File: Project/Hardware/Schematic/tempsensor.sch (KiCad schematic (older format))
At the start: 0 parts

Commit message: Lade till krets för temperatursensor.
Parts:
- added C?: 0.1u, symbol Device:C
- added R? (x6): R, symbol Device:R
- added TH?: PT1000, symbol Sensor_Temperature:PT1000
- added U?: MAX4460ESA+, 21-0041B_8, symbol PASC:MAX4460ESA+
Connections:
- new net: R?.2, TH?.1
- new net +3V3: C?.1, R?.1, R?.2, U?.7 (VDD)
- new net GND: C?.2, R?.1, R?.2, TH?.2, U?.2 (GND)
- new net INAMPFB: R?.1, R?.2, U?.8 (FB)
- new net TEMPOUT: R?.1, U?.1 (OUT)
- new net WBRIDGE+: R?.1, R?.1, U?.3 (IN+)
- new net WBRIDGE-: R?.2, R?.2, U?.6 (IN-)
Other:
- note added: "Instrumentation Amplifier"
- note added: "Set gain: 1 + R2/R1; R1 + R2 approx. = 100k\nR2 between OUT and FB,\nR1 between FB and GND."
- note added: "Wheatstone Bridge for Pt1000 thermistor.\n"

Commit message: Lade till komponentvärden i kretsschemat för temperatursensorkretsen
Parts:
- added R? (x2): 270k, symbol Device:R
- added R?: 820, symbol Device:R
- R?: value R -> 1k
- R? (x2): value R -> 8.2k
- R?: value R -> 1.8k
- R?: value R -> 100k
- R?: value R -> 2.7k
- U?: symbol PASC:MAX4460ESA+ -> lab-rescue:MAX4460ESA+-PASC
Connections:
- net +3V3: now also R?.1, R?.2
- net GND: now also R?.2; no longer R?.2
- net WBRIDGE+: now also R?.1
- net WBRIDGE-: now also R?.2
- new net: R?.1, R?.2
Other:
- moved on the sheet: R?, TH?
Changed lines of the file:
@@
 L Sensor_Temperature:PT1000 TH?
 U 1 1 5C561FEF
-P 3000 2600
-F 0 "TH?" H 3098 2646 50  0000 L CNN
-F 1 "PT1000" H 3098 2555 50  0000 L CNN
-F 2 "" H 3000 2650 50  0001 C CNN
-F 3 "https://www.heraeus.com/media/media/group/doc_group/products_1/hst/sot_to/de_15/to_92_d.pdf" H 3000 2650 50  0001 C CNN
-	1    3000 2600
+P 3200 2600
+F 0 "TH?" H 3298 2646 50  0000 L CNN
+F 1 "PT1000" H 3298 2555 50  0000 L CNN
+F 2 "" H 3200 2650 50  0001 C CNN
+F 3 "https://www.heraeus.com/media/media/group/doc_group/products_1/hst/sot_to/de_15/to_92_d.pdf" H 3200 2650 50  0001 C CNN
+	1    3200 2600
 	1    0    0    -1
 $EndComp
@@
 L Device:R R?
 U 1 1 5C5621D5
-P 3000 2200
-F 0 "R?" H 3070 2246 50  0000 L CNN
-F 1 "R" H 3070 2155 50  0000 L CNN
-F 2 "" V 2930 2200 50  0001 C CNN
-F 3 "~" H 3000 2200 50  0001 C CNN
-	1    3000 2200
+P 3200 2200
+F 0 "R?" H 3270 2246 50  0000 L CNN
+F 1 "1k" H 3270 2155 50  0000 L CNN
+F 2 "" V 3130 2200 50  0001 C CNN
+F 3 "~" H 3200 2200 50  0001 C CNN
+	1    3200 2200
 	1    0    0    -1
 $EndComp
@@
 L Device:R R?
 U 1 1 5C5622D1
-P 2400 2600
-F 0 "R?" H 2470 2646 50  0000 L CNN
-F 1 "R" H 2470 2555 50  0000 L CNN
-F 2 "" V 2330 2600 50  0001 C CNN
-F 3 "~" H 2400 2600 50  0001 C CNN
-	1    2400 2600
+P 1900 2600
+F 0 "R?" H 1970 2646 50  0000 L CNN
+F 1 "8.2k" H 1970 2555 50  0000 L CNN
+F 2 "" V 1830 2600 50  0001 C CNN
+F 3 "~" H 1900 2600 50  0001 C CNN
+	1    1900 2600
 	1    0    0    -1
 $EndComp
@@
 L Device:R R?
 U 1 1 5C562312
-P 3000 3200
-F 0 "R?" H 3070 3246 50  0000 L CNN
-F 1 "R" H 3070 3155 50  0000 L CNN
-F 2 "" V 2930 3200 50  0001 C CNN
-F 3 "~" H 3000 3200 50  0001 C CNN
-	1    3000 3200
+P 3200 3200
+F 0 "R?" H 3270 3246 50  0000 L CNN
+F 1 "1.8k" H 3270 3155 50  0000 L CNN
+F 2 "" V 3130 3200 50  0001 C CNN
+F 3 "~" H 3200 3200 50  0001 C CNN
+	1    3200 3200
 	1    0    0    -1
 $EndComp
@@
 L Device:R R?
 U 1 1 5C56234C
-P 2400 3200
-F 0 "R?" H 2470 3246 50  0000 L CNN
-F 1 "R" H 2470 3155 50  0000 L CNN
-F 2 "" V 2330 3200 50  0001 C CNN
-F 3 "~" H 2400 3200 50  0001 C CNN
-	1    2400 3200
-	1    0    0    -1
-$EndComp
-$Comp
-L PASC:MAX4460ESA+ U?
+P 1900 3200
+F 0 "R?" H 1970 3246 50  0000 L CNN
+F 1 "8.2k" H 1970 3155 50  0000 L CNN
+F 2 "" V 1830 3200 50  0001 C CNN
+F 3 "~" H 1900 3200 50  0001 C CNN
+	1    1900 3200
+	1    0    0    -1
+$EndComp
+$Comp
+L lab-rescue:MAX4460ESA+-PASC U?
 U 1 1 5C562619
 P 5000 2100
+AR Path="/5C562619" Ref="U?"  Part="1"
+AR Path="/5C564F10/5C562619" Ref="U?"  Part="1"
 F 0 "U?" H 6100 2487 60  0000 C CNN
 F 1 "MAX4460ESA+" H 6100 2381 60  0000 C CNN
@@
 L power:+3V3 #PWR?
 U 1 1 5C5626CF
-P 2100 2700
-F 0 "#PWR?" H 2100 2550 50  0001 C CNN
-F 1 "+3V3" H 2115 2873 50  0000 C CNN
-F 2 "" H 2100 2700 50  0001 C CNN
-F 3 "" H 2100 2700 50  0001 C CNN
-	1    2100 2700
-	1    0    0    -1
-$EndComp
-Wire Wire Line
-	2100 2700 2100 2900
-Wire Wire Line
-	2100 2900 2400 2900
-Wire Wire Line
-	2400 2900 2400 2750
-Wire Wire Line
-	2400 2900 2400 3050
-Connection ~ 2400 2900
-Wire Wire Line
-	2400 3350 2400 3500
-Wire Wire Line
-	2400 3500 3000 3500
-Wire Wire Line
-	3000 3500 3000 3350
-Wire Wire Line
-	3000 3050 3000 2900
-Wire Wire Line
-	2400 2450 2400 1900
-Wire Wire Line
-	2400 1900 3000 1900
-Wire Wire Line
-	3000 2350 3000 2450
+P 1600 2700
+F 0 "#PWR?" H 1600 2550 50  0001 C CNN
+F 1 "+3V3" H 1615 2873 50  0000 C CNN
+F 2 "" H 1600 2700 50  0001 C CNN
+F 3 "" H 1600 2700 50  0001 C CNN
+	1    1600 2700
+	1    0    0    -1
+$EndComp
+Wire Wire Line
+	1600 2700 1600 2900
+Wire Wire Line
+	1600 2900 1900 2900
+Wire Wire Line
+	1900 2900 1900 2750
+Wire Wire Line
+	1900 2900 1900 3050
+Connection ~ 1900 2900
+Wire Wire Line
+	1900 3350 1900 3500
+Wire Wire Line
+	1900 3500 2300 3500
+Wire Wire Line
+	3200 3500 3200 3350
+Wire Wire Line
+	3200 3050 3200 2900
+Wire Wire Line
+	1900 2450 1900 1900
+Wire Wire Line
+	1900 1900 2300 1900
+Wire Wire Line
+	3200 2350 3200 2450
 $Comp
 L power:GND #PWR?
 U 1 1 5C562A08
-P 3300 3100
-F 0 "#PWR?" H 3300 2850 50  0001 C CNN
-F 1 "GND" H 3305 2927 50  0000 C CNN
-F 2 "" H 3300 3100 50  0001 C CNN
-F 3 "" H 3300 3100 50  0001 C CNN
-	1    3300 3100
-	1    0    0    -1
-$EndComp
-Wire Wire Line
-	3300 3100 3300 2900
-Wire Wire Line
-	3300 2900 3000 2900
-Connection ~ 3000 2900
-Wire Wire Line
-	3000 2900 3000 2750
-Wire Wire Line
-	3000 1900 3000 2050
-Wire Wire Line
-	3000 1900 3500 1900
-Connection ~ 3000 1900
-Wire Wire Line
-	3500 3500 3000 3500
-Connection ~ 3000 3500
-Text Label 3500 3500 0    50   ~ 0
+P 3600 3050
+F 0 "#PWR?" H 3600 2800 50  0001 C CNN
+F 1 "GND" H 3605 2877 50  0000 C CNN
+F 2 "" H 3600 3050 50  0001 C CNN
+F 3 "" H 3600 3050 50  0001 C CNN
+	1    3600 3050
+	1    0    0    -1
+$EndComp
+Wire Wire Line
+	3600 3050 3600 2900
+Wire Wire Line
+	3600 2900 3200 2900
+Connection ~ 3200 2900
+Wire Wire Line
+	3200 2900 3200 2750
+Wire Wire Line
+	3200 1900 3200 2050
+Wire Wire Line
+	3200 1900 3700 1900
+Connection ~ 3200 1900
+Wire Wire Line
+	3700 3500 3200 3500
+Connection ~ 3200 3500
+Text Label 3700 3500 0    50   ~ 0
 WBRIDGE-
-Text Label 3500 1900 0    50   ~ 0
+Text Label 3700 1900 0    50   ~ 0
 WBRIDGE+
 Text Label 5000 2300 2    50   ~ 0
@@
 P 4600 3700
 F 0 "R?" H 4670 3746 50  0000 L CNN
-F 1 "R" H 4670 3655 50  0000 L CNN
+F 1 "100k" H 4670 3655 50  0000 L CNN
 F 2 "" V 4530 3700 50  0001 C CNN
 F 3 "~" H 4600 3700 50  0001 C CNN
@@
 P 4600 4100
 F 0 "R?" H 4670 4146 50  0000 L CNN
-F 1 "R" H 4670 4055 50  0000 L CNN
+F 1 "2.7k" H 4670 4055 50  0000 L CNN
 F 2 "" V 4530 4100 50  0001 C CNN
 F 3 "~" H 4600 4100 50  0001 C CNN
@@
 Wire Wire Line
 	4600 3850 4600 3900
-Wire Wire Line
-	4600 4250 4600 4300
 Wire Wire Line
 	4600 3900 4800 3900
@@
 L power:GND #PWR?
 U 1 1 5C5640C7
-P 4600 4300
-F 0 "#PWR?" H 4600 4050 50  0001 C CNN
-F 1 "GND" H 4605 4127 50  0000 C CNN
-F 2 "" H 4600 4300 50  0001 C CNN
-F 3 "" H 4600 4300 50  0001 C CNN
-	1    4600 4300
+P 4600 4750
+F 0 "#PWR?" H 4600 4500 50  0001 C CNN
+F 1 "GND" H 4605 4577 50  0000 C CNN
+F 2 "" H 4600 4750 50  0001 C CNN
+F 3 "" H 4600 4750 50  0001 C CNN
+	1    4600 4750
 	1    0    0    -1
 $EndComp
@@
 	4400 3300 7100 3300
 Wire Notes Line
-	7100 3300 7100 4600
-Wire Notes Line
-	7100 4600 4400 4600
-Wire Notes Line
-	4400 4600 4400 3300
+	7100 3300 7100 5100
+Wire Notes Line
+	7100 5100 4400 5100
+Wire Notes Line
+	4400 5100 4400 3300
 $Comp
 L power:+3V3 #PWR?
@@
 Text Notes 4700 1600 0    50   ~ 0
 Instrumentation Amplifier
-Text Notes 2100 1600 0    50   ~ 0
+Text Notes 1500 1600 0    50   ~ 0
 Wheatstone Bridge for Pt1000 thermistor.\n
 $Comp
@@
 	4400 1400 4400 3200
 Wire Notes Line
-	4000 1400 1900 1400
-Wire Notes Line
-	1900 1400 1900 3700
-Wire Notes Line
-	1900 3700 4000 3700
-Wire Notes Line
-	4000 3700 4000 1400
+	4200 1400 1300 1400
+Wire Notes Line
+	1300 1400 1300 3700
+Wire Notes Line
+	1300 3700 4200 3700
+Wire Notes Line
+	4200 3700 4200 1400
+$Comp
+L Device:R R?
+U 1 1 5C58B777
+P 2300 2600
+F 0 "R?" H 2370 2646 50  0000 L CNN
+F 1 "270k" H 2370 2555 50  0000 L CNN
+F 2 "" V 2230 2600 50  0001 C CNN
+F 3 "~" H 2300 2600 50  0001 C CNN
+	1    2300 2600
+	1    0    0    -1
+$EndComp
+$Comp
+L Device:R R?
+U 1 1 5C58B7A7
+P 2300 3200
+F 0 "R?" H 2370 3246 50  0000 L CNN
+F 1 "270k" H 2370 3155 50  0000 L CNN
+F 2 "" V 2230 3200 50  0001 C CNN
+F 3 "~" H 2300 3200 50  0001 C CNN
+	1    2300 3200
+	1    0    0    -1
+$EndComp
+$Comp
+L Device:R R?
+U 1 1 5C58C2D0
+P 4600 4500
+F 0 "R?" H 4670 4546 50  0000 L CNN
+F 1 "820" H 4670 4455 50  0000 L CNN
+F 2 "" V 4530 4500 50  0001 C CNN
+F 3 "~" H 4600 4500 50  0001 C CNN
+	1    4600 4500
+	1    0    0    -1
+$EndComp
+Wire Wire Line
+	4600 4350 4600 4250
+Wire Wire Line
+	4600 4650 4600 4750
+Wire Wire Line
+	2300 3500 2300 3350
+Connection ~ 2300 3500
+Wire Wire Line
+	2300 3500 3200 3500
+Wire Wire Line
+	2300 3050 2300 2900
+Wire Wire Line
+	1900 2900 2300 2900
+Connection ~ 2300 2900
+Wire Wire Line
+	2300 2900 2300 2750
+Wire Wire Line
+	2300 2450 2300 1900
+Connection ~ 2300 1900
+Wire Wire Line
+	2300 1900 3200 1900
 $EndSCHEMATC

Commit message: Pulse, piezo och labels (#8)
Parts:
- U?: symbol lab-rescue:MAX4460ESA+-PASC -> PASC:MAX4460ESA+
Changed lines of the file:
@@
 $EndComp
 $Comp
-L lab-rescue:MAX4460ESA+-PASC U?
+L PASC:MAX4460ESA+ U?
 U 1 1 5C562619
 P 5000 2100
@@
 Text Label 7200 2100 0    50   ~ 0
 INAMPFB
-Text Label 5000 2100 2    50   ~ 0
-TEMPOUT
 $Comp
 L Device:R R?
@@
 Wire Wire Line
 	2300 1900 3200 1900
+Text HLabel 5000 2100 0    50   Input ~ 0
+TEMPOUT
 $EndSCHEMATC

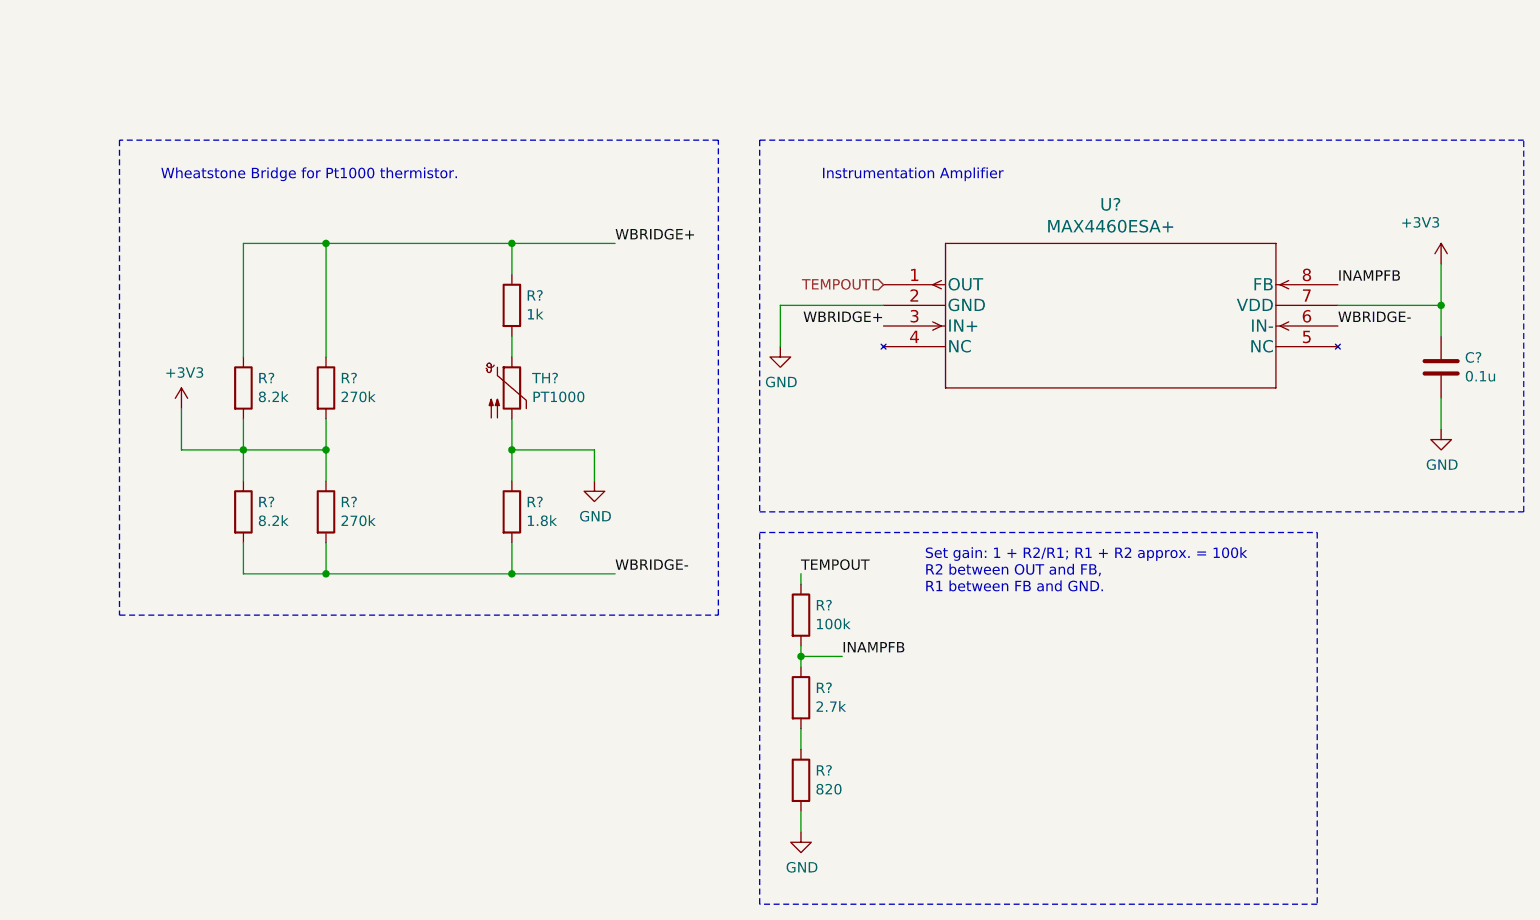
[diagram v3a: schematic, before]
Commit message: Tog bort power supply +7, lade till switch för att switcha mellan batteri och USB power. Lade till power-net symbol för oregulerad supply voltage +VIN.
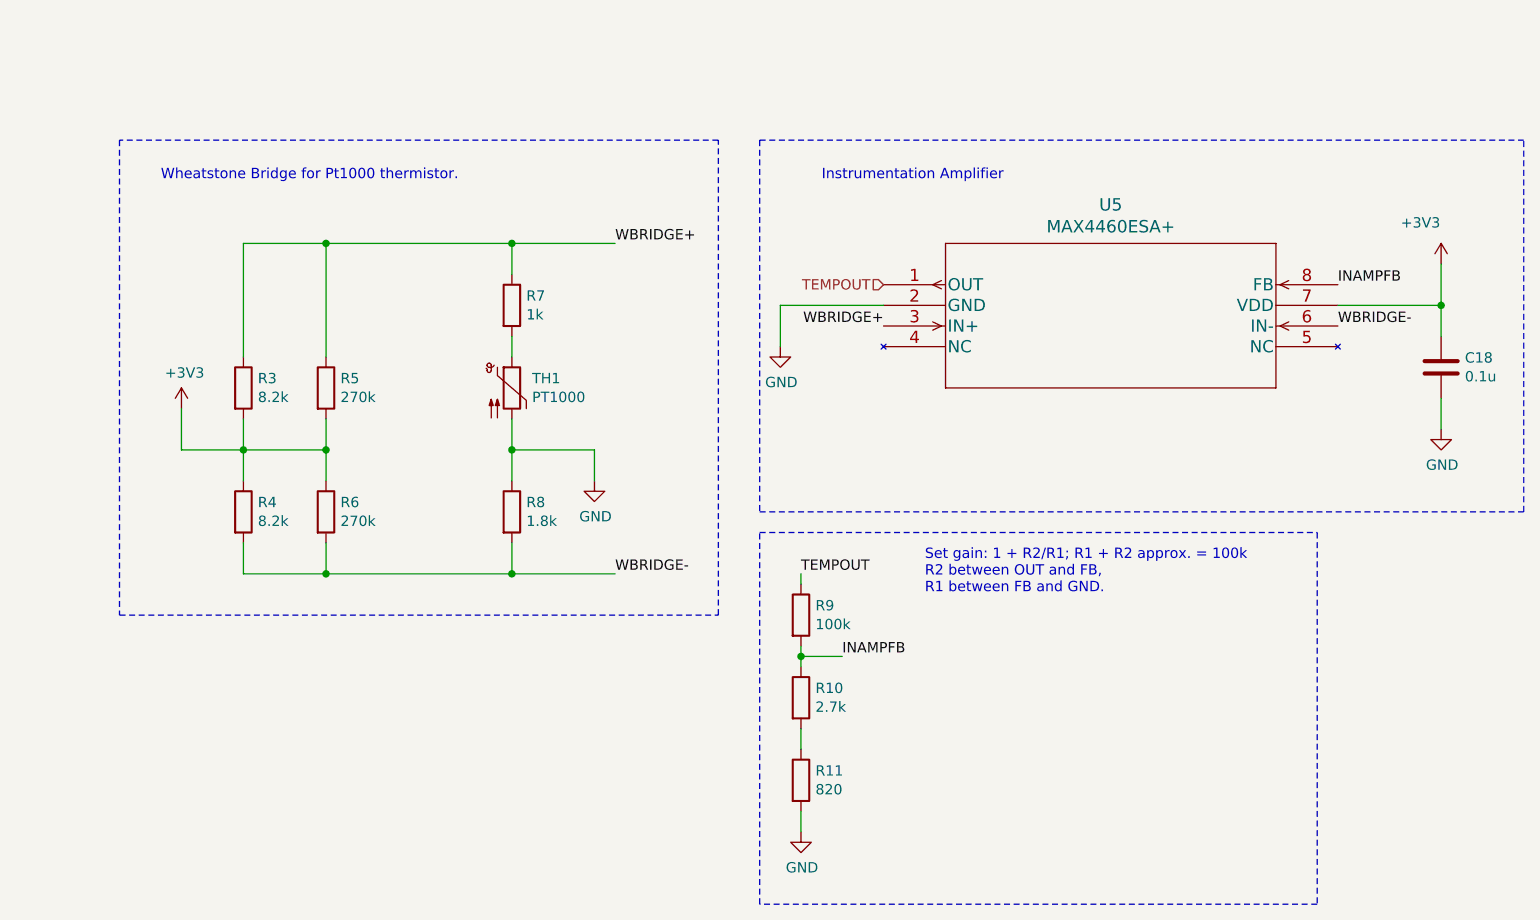
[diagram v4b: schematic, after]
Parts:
- gave numbers to parts that had none: 12
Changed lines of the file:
@@
 $EndDescr
 $Comp
-L Sensor_Temperature:PT1000 TH?
+L Sensor_Temperature:PT1000 TH1
 U 1 1 5C561FEF
 P 3200 2600
-F 0 "TH?" H 3298 2646 50  0000 L CNN
+F 0 "TH1" H 3298 2646 50  0000 L CNN
 F 1 "PT1000" H 3298 2555 50  0000 L CNN
 F 2 "" H 3200 2650 50  0001 C CNN
@@
 $EndComp
 $Comp
-L Device:R R?
+L Device:R R7
 U 1 1 5C5621D5
 P 3200 2200
-F 0 "R?" H 3270 2246 50  0000 L CNN
+F 0 "R7" H 3270 2246 50  0000 L CNN
 F 1 "1k" H 3270 2155 50  0000 L CNN
 F 2 "" V 3130 2200 50  0001 C CNN
@@
 $EndComp
 $Comp
-L Device:R R?
+L Device:R R3
 U 1 1 5C5622D1
 P 1900 2600
-F 0 "R?" H 1970 2646 50  0000 L CNN
+F 0 "R3" H 1970 2646 50  0000 L CNN
 F 1 "8.2k" H 1970 2555 50  0000 L CNN
 F 2 "" V 1830 2600 50  0001 C CNN
@@
 $EndComp
 $Comp
-L Device:R R?
+L Device:R R8
 U 1 1 5C562312
 P 3200 3200
-F 0 "R?" H 3270 3246 50  0000 L CNN
+F 0 "R8" H 3270 3246 50  0000 L CNN
 F 1 "1.8k" H 3270 3155 50  0000 L CNN
 F 2 "" V 3130 3200 50  0001 C CNN
@@
 $EndComp
 $Comp
-L Device:R R?
+L Device:R R4
 U 1 1 5C56234C
 P 1900 3200
-F 0 "R?" H 1970 3246 50  0000 L CNN
+F 0 "R4" H 1970 3246 50  0000 L CNN
 F 1 "8.2k" H 1970 3155 50  0000 L CNN
 F 2 "" V 1830 3200 50  0001 C CNN
@@
 P 5000 2100
 AR Path="/5C562619" Ref="U?"  Part="1"
-AR Path="/5C564F10/5C562619" Ref="U?"  Part="1"
-F 0 "U?" H 6100 2487 60  0000 C CNN
+AR Path="/5C564F10/5C562619" Ref="U5"  Part="1"
+F 0 "U5" H 6100 2487 60  0000 C CNN
 F 1 "MAX4460ESA+" H 6100 2381 60  0000 C CNN
 F 2 "21-0041B_8" H 6100 2340 60  0001 C CNN
@@
 $EndComp
 $Comp
-L power:+3V3 #PWR?
+L power:+3V3 #PWR0128
 U 1 1 5C5626CF
 P 1600 2700
-F 0 "#PWR?" H 1600 2550 50  0001 C CNN
+F 0 "#PWR0128" H 1600 2550 50  0001 C CNN
 F 1 "+3V3" H 1615 2873 50  0000 C CNN
 F 2 "" H 1600 2700 50  0001 C CNN
@@
 	3200 2350 3200 2450
 $Comp
-L power:GND #PWR?
+L power:GND #PWR0129
 U 1 1 5C562A08
 P 3600 3050
-F 0 "#PWR?" H 3600 2800 50  0001 C CNN
+F 0 "#PWR0129" H 3600 2800 50  0001 C CNN
 F 1 "GND" H 3605 2877 50  0000 C CNN
 F 2 "" H 3600 3050 50  0001 C CNN
@@
 INAMPFB
 $Comp
-L Device:R R?
+L Device:R R9
 U 1 1 5C5639FE
 P 4600 3700
-F 0 "R?" H 4670 3746 50  0000 L CNN
+F 0 "R9" H 4670 3746 50  0000 L CNN
 F 1 "100k" H 4670 3655 50  0000 L CNN
 F 2 "" V 4530 3700 50  0001 C CNN
@@
 $EndComp
 $Comp
-L Device:R R?
+L Device:R R10
 U 1 1 5C563A36
 P 4600 4100
-F 0 "R?" H 4670 4146 50  0000 L CNN
+F 0 "R10" H 4670 4146 50  0000 L CNN
 F 1 "2.7k" H 4670 4055 50  0000 L CNN
 F 2 "" V 4530 4100 50  0001 C CNN
@@
 TEMPOUT
 $Comp
-L power:GND #PWR?
+L power:GND #PWR0130
 U 1 1 5C5640C7
 P 4600 4750
-F 0 "#PWR?" H 4600 4500 50  0001 C CNN
+F 0 "#PWR0130" H 4600 4500 50  0001 C CNN
 F 1 "GND" H 4605 4577 50  0000 C CNN
 F 2 "" H 4600 4750 50  0001 C CNN
@@
 	4400 5100 4400 3300
 $Comp
-L power:+3V3 #PWR?
+L power:+3V3 #PWR0131
 U 1 1 5C56452F
 P 7700 2000
-F 0 "#PWR?" H 7700 1850 50  0001 C CNN
+F 0 "#PWR0131" H 7700 1850 50  0001 C CNN
 F 1 "+3V3" H 7600 2200 50  0000 C CNN
 F 2 "" H 7700 2000 50  0001 C CNN
@@
 	7700 2200 7200 2200
 $Comp
-L power:GND #PWR?
+L power:GND #PWR0132
 U 1 1 5C564858
 P 4500 2400
-F 0 "#PWR?" H 4500 2150 50  0001 C CNN
+F 0 "#PWR0132" H 4500 2150 50  0001 C CNN
 F 1 "GND" H 4505 2227 50  0000 C CNN
 F 2 "" H 4500 2400 50  0001 C CNN
@@
 Wheatstone Bridge for Pt1000 thermistor.\n
 $Comp
-L Device:C C?
+L Device:C C18
 U 1 1 5C565EBC
 P 7700 2500
-F 0 "C?" H 7815 2546 50  0000 L CNN
+F 0 "C18" H 7815 2546 50  0000 L CNN
 F 1 "0.1u" H 7815 2455 50  0000 L CNN
 F 2 "" H 7738 2350 50  0001 C CNN
@@
 Connection ~ 7700 2200
 $Comp
-L power:GND #PWR?
+L power:GND #PWR0133
 U 1 1 5C5665E0
 P 7700 2800
-F 0 "#PWR?" H 7700 2550 50  0001 C CNN
+F 0 "#PWR0133" H 7700 2550 50  0001 C CNN
 F 1 "GND" H 7705 2627 50  0000 C CNN
 F 2 "" H 7700 2800 50  0001 C CNN
@@
 	4200 3700 4200 1400
 $Comp
-L Device:R R?
+L Device:R R5
 U 1 1 5C58B777
 P 2300 2600
-F 0 "R?" H 2370 2646 50  0000 L CNN
+F 0 "R5" H 2370 2646 50  0000 L CNN
 F 1 "270k" H 2370 2555 50  0000 L CNN
 F 2 "" V 2230 2600 50  0001 C CNN
@@
 $EndComp
 $Comp
-L Device:R R?
+L Device:R R6
 U 1 1 5C58B7A7
 P 2300 3200
-F 0 "R?" H 2370 3246 50  0000 L CNN
+F 0 "R6" H 2370 3246 50  0000 L CNN
 F 1 "270k" H 2370 3155 50  0000 L CNN
 F 2 "" V 2230 3200 50  0001 C CNN
@@
 $EndComp
 $Comp
-L Device:R R?
+L Device:R R11
 U 1 1 5C58C2D0
 P 4600 4500
-F 0 "R?" H 4670 4546 50  0000 L CNN
+F 0 "R11" H 4670 4546 50  0000 L CNN
 F 1 "820" H 4670 4455 50  0000 L CNN
 F 2 "" V 4530 4500 50  0001 C CNN

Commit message: Intermediate...
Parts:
- C18: value 0.1u -> 100n; footprint (none) -> Capacitor_SMD:C_0805_2012Metric_Pad1.15x1.40mm_HandSolder
- R10, R11, R3, R4, R5, R6, R7, R8, R9: footprint (none) -> Resistor_SMD:R_0805_2012Metric_Pad1.15x1.40mm_HandSolder
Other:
- moved on the sheet: C18, R10, R11, R3, R4, R5, R6, R7, R8, R9, TH1, U5

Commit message: Lade till vippströmställare footprint och uppdaterade max4460 footprint för att det förhoppningsvis ska laddas av alla
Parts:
- TH1: footprint (none) -> Resistor_THT:R_Axial_DIN0204_L3.6mm_D1.6mm_P2.54mm_Vertical
- U5: footprint 21-0041B_8 -> PASC:MAX4460ESA+
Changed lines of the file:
@@
 F 0 "TH1" H 2798 2046 50  0000 L CNN
 F 1 "PT1000" H 2798 1955 50  0000 L CNN
-F 2 "" H 2700 2050 50  0001 C CNN
+F 2 "Resistor_THT:R_Axial_DIN0204_L3.6mm_D1.6mm_P2.54mm_Vertical" H 2700 2050 50  0001 C CNN
 F 3 "https://www.heraeus.com/media/media/group/doc_group/products_1/hst/sot_to/de_15/to_92_d.pdf" H 2700 2050 50  0001 C CNN
 	1    2700 2000
@@
 F 0 "U5" H 5600 1887 60  0000 C CNN
 F 1 "MAX4460ESA+" H 5600 1781 60  0000 C CNN
-F 2 "21-0041B_8" H 5600 1740 60  0001 C CNN
+F 2 "PASC:MAX4460ESA+" H 5600 1740 60  0001 C CNN
 F 3 "" H 4500 1500 60  0000 C CNN
 	1    4500 1500
